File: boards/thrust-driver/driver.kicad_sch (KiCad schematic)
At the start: 33 parts, among them J1 HELM J13 1:1, J2 LUG BATT+, J3 LUG BATT-, J4 LUG MOT A, J5 LUG MOT B, J6 CAN XCVR 3V3, J7 NMEA2000 PWR, U1 BTN8982TA, U2 BTN8982TA, U3 BTN8982TA, U4 BTN8982TA, U5 Pico 2 (DNP), U6 R-78E5.0-0.5 (DNP)

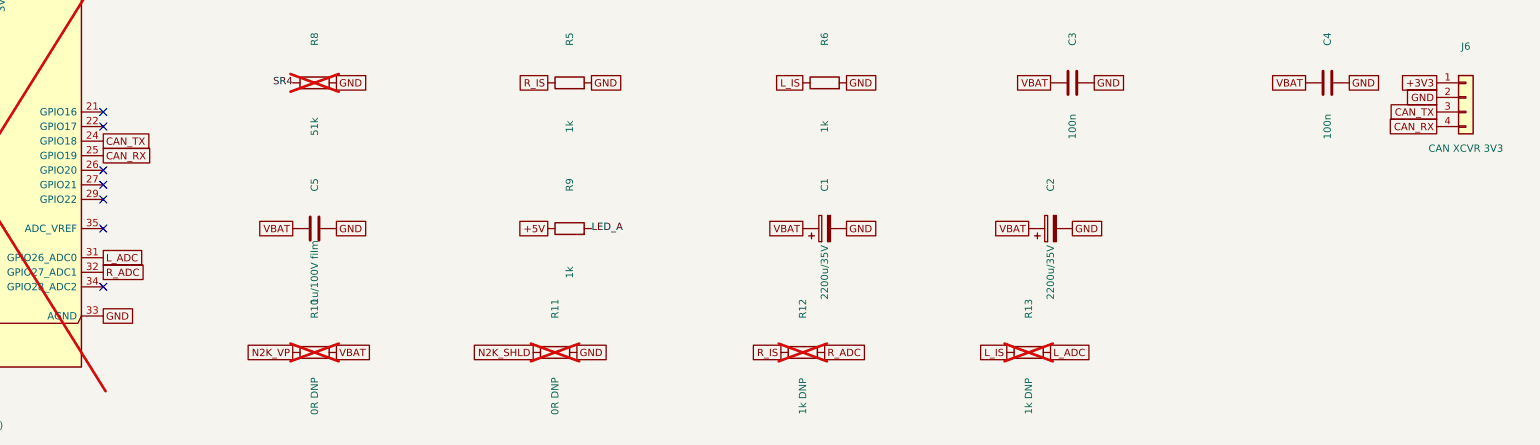
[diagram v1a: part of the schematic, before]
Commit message: feat(schematics): wire the Pico to its peripherals on both boards
Helm control page: GP0-3 bus to J12, 4-wire thrust bus to J13 (nested
staircase under the pico), RPWM/LPWM to the servo bridge inputs,
LED_STAT to R13, VBAT_SENSE over the arrivals down to the divider rail.
Driver page: DNP-pico CAN pair to J6, IS-to-ADC series R12/R13.
gen_sheet.py: turtle-style waypoint routing for WIRES (("x"/"y", v)
segments + auto-L tail); layout shuffle so J12/J13 flank the pico.

Co-Authored-By: Claude Fable 5 <noreply@anthropic.com>
Claude-Session: https://claude.ai/code/session_011PT4Xv5KGhDdDc8nqJyMxJ
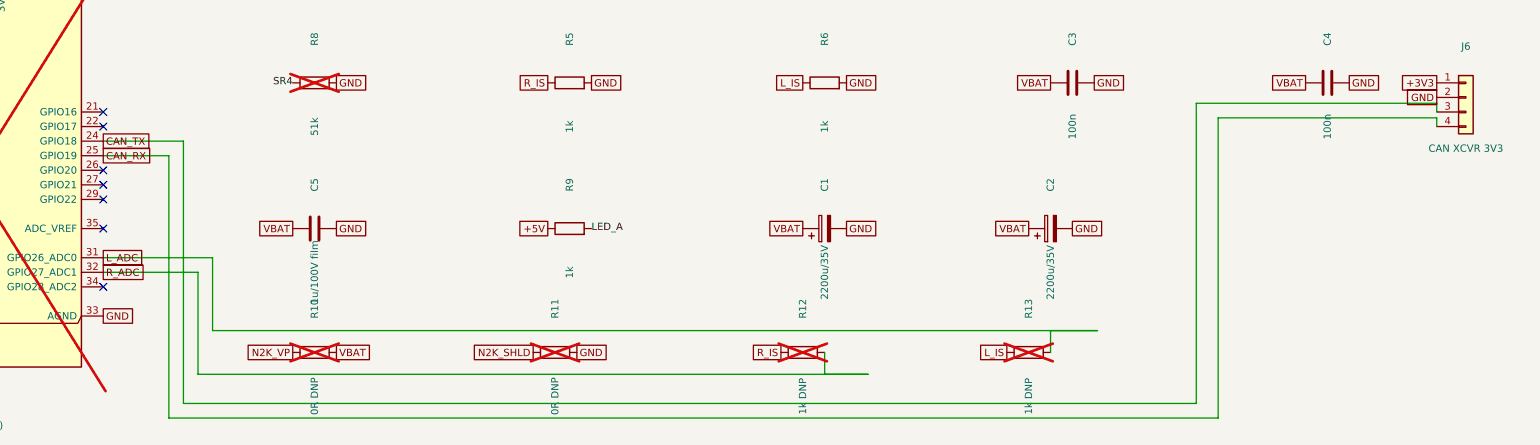
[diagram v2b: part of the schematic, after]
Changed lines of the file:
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@@
     (instances (project "vanchor-thrust" (path "/d0000000-0000-4000-8000-000000000001/d0000000-0000-4000-8000-000000000002" (reference "#FLG03") (unit 1))))
   )
+  (wire (pts (xy 92.71 229.87) (xy 106.68 229.87))
+    (stroke (width 0) (type default)))
+  (wire (pts (xy 106.68 229.87) (xy 106.68 275.59))
+    (stroke (width 0) (type default)))
+  (wire (pts (xy 106.68 275.59) (xy 283.21 275.59))
+    (stroke (width 0) (type default)))
+  (wire (pts (xy 283.21 275.59) (xy 283.21 223.27))
+    (stroke (width 0) (type default)))
+  (wire (pts (xy 283.21 223.27) (xy 325.12 223.27))
+    (stroke (width 0) (type default)))
+  (wire (pts (xy 325.12 223.27) (xy 325.12 224.79))
+    (stroke (width 0) (type default)))
+  (wire (pts (xy 92.71 232.41) (xy 104.14 232.41))
+    (stroke (width 0) (type default)))
+  (wire (pts (xy 104.14 232.41) (xy 104.14 278.13))
+    (stroke (width 0) (type default)))
+  (wire (pts (xy 104.14 278.13) (xy 287.02 278.13))
+    (stroke (width 0) (type default)))
+  (wire (pts (xy 287.02 278.13) (xy 287.02 225.81))
+    (stroke (width 0) (type default)))
+  (wire (pts (xy 287.02 225.81) (xy 325.12 225.81))
+    (stroke (width 0) (type default)))
+  (wire (pts (xy 325.12 225.81) (xy 325.12 227.33))
+    (stroke (width 0) (type default)))
+  (wire (pts (xy 92.71 250.19) (xy 111.76 250.19))
+    (stroke (width 0) (type default)))
+  (wire (pts (xy 111.76 250.19) (xy 111.76 262.89))
+    (stroke (width 0) (type default)))
+  (wire (pts (xy 111.76 262.89) (xy 266 262.89))
+    (stroke (width 0) (type default)))
+  (wire (pts (xy 266 262.89) (xy 257.81 262.89))
+    (stroke (width 0) (type default)))
+  (wire (pts (xy 257.81 262.89) (xy 257.81 266.7))
+    (stroke (width 0) (type default)))
+  (wire (pts (xy 92.71 252.73) (xy 109.22 252.73))
+    (stroke (width 0) (type default)))
+  (wire (pts (xy 109.22 252.73) (xy 109.22 270.51))
+    (stroke (width 0) (type default)))
+  (wire (pts (xy 109.22 270.51) (xy 226 270.51))
+    (stroke (width 0) (type default)))
+  (wire (pts (xy 226 270.51) (xy 218.44 270.51))
+    (stroke (width 0) (type default)))
+  (wire (pts (xy 218.44 270.51) (xy 218.44 266.7))
+    (stroke (width 0) (type default)))
   (global_label "RPWM" (shape passive) (at 39.37 87.63 180.0) (fields_autoplaced yes)
     (effects (font (size 1.27 1.27)) (justify right))
@@
       (effects (font (size 1.27 1.27)) (hide yes)))
   )
-  (global_label "CAN_TX" (shape passive) (at 325.12 224.79 180.0) (fields_autoplaced yes)
-    (effects (font (size 1.27 1.27)) (justify right))
-    (property "Intersheetrefs" "${INTERSHEET_REFS}" (at 325.12 224.79 0)
-      (effects (font (size 1.27 1.27)) (hide yes)))
-  )
-  (global_label "CAN_RX" (shape passive) (at 325.12 227.33 180.0) (fields_autoplaced yes)
-    (effects (font (size 1.27 1.27)) (justify right))
-    (property "Intersheetrefs" "${INTERSHEET_REFS}" (at 325.12 227.33 0)
-      (effects (font (size 1.27 1.27)) (hide yes)))
-  )
   (global_label "N2K_VP" (shape passive) (at 368.3 219.71 180.0) (fields_autoplaced yes)
     (effects (font (size 1.27 1.27)) (justify right))
@@
       (effects (font (size 1.27 1.27)) (hide yes)))
   )
-  (global_label "R_ADC" (shape passive) (at 218.44 266.7 0.0) (fields_autoplaced yes)
-    (effects (font (size 1.27 1.27)) (justify left))
-    (property "Intersheetrefs" "${INTERSHEET_REFS}" (at 218.44 266.7 0)
-      (effects (font (size 1.27 1.27)) (hide yes)))
-  )
   (global_label "L_IS" (shape passive) (at 250.19 266.7 180.0) (fields_autoplaced yes)
     (effects (font (size 1.27 1.27)) (justify right))
@@
       (effects (font (size 1.27 1.27)) (hide yes)))
   )
-  (global_label "L_ADC" (shape passive) (at 257.81 266.7 0.0) (fields_autoplaced yes)
-    (effects (font (size 1.27 1.27)) (justify left))
-    (property "Intersheetrefs" "${INTERSHEET_REFS}" (at 257.81 266.7 0)
-      (effects (font (size 1.27 1.27)) (hide yes)))
-  )

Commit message: fix(schematics): visual QA pass — text collisions and wire-through-symbol
gen_sheet: BAT54S ref+value stack below the part (COM pin label owns the
space above — fixes D8/D10/D11/D14 overprinted refs); REF_POS per-part
ref override. Carrier: F1->Q1 drain wire enters from above instead of
through the FET symbol; Q1 ref moved clear. Control: R20/R21 spread so
their texts don't merge; D14 lifted off the VBAT wire; LED_STAT run
raised above the pico power flags. Driver: ADC wires lose their dead-end
spurs; CAN lanes dropped below the DNP value texts; D2 horizontal (label
was overprinting ref/value). HANDOFF: waive note for the 3 paralleled-OUT
ERC errors. Netlists verified identical on both boards.

Co-Authored-By: Claude Fable 5 <noreply@anthropic.com>
Claude-Session: https://claude.ai/code/session_011PT4Xv5KGhDdDc8nqJyMxJ
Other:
- moved on the sheet: D2
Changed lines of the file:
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@@
     (instances (project "vanchor-thrust" (path "/d0000000-0000-4000-8000-000000000001/d0000000-0000-4000-8000-000000000002" (reference "R6") (unit 1))))
   )
-  (symbol (lib_id "Device:D_TVS") (at 330.2 191.77 90) (unit 1)
-    (exclude_from_sim no) (in_bom yes) (on_board yes) (dnp no)
-    (property "Reference" "D2" (at 330.2 184.15 0)
-      (effects (font (size 1.27 1.27))))
-    (property "Value" "SMCJ33A" (at 330.2 199.39 0)
-      (effects (font (size 1.27 1.27))))
-    (property "Footprint" "Diode_SMD:D_SMC" (at 330.2 191.77 0)
-      (effects (font (size 1.27 1.27)) (hide yes)))
-    (property "Datasheet" "" (at 330.2 191.77 0)
+  (symbol (lib_id "Device:D_TVS") (at 322.58 190.5 0) (unit 1)
+    (exclude_from_sim no) (in_bom yes) (on_board yes) (dnp no)
+    (property "Reference" "D2" (at 322.58 182.88 0)
+      (effects (font (size 1.27 1.27))))
+    (property "Value" "SMCJ33A" (at 322.58 198.12 0)
+      (effects (font (size 1.27 1.27))))
+    (property "Footprint" "Diode_SMD:D_SMC" (at 322.58 190.5 0)
+      (effects (font (size 1.27 1.27)) (hide yes)))
+    (property "Datasheet" "" (at 322.58 190.5 0)
       (effects (font (size 1.27 1.27)) (hide yes)))
     (pin "1")
@@
   (wire (pts (xy 92.71 229.87) (xy 106.68 229.87))
     (stroke (width 0) (type default)))
-  (wire (pts (xy 106.68 229.87) (xy 106.68 275.59))
-    (stroke (width 0) (type default)))
-  (wire (pts (xy 106.68 275.59) (xy 283.21 275.59))
-    (stroke (width 0) (type default)))
-  (wire (pts (xy 283.21 275.59) (xy 283.21 223.27))
+  (wire (pts (xy 106.68 229.87) (xy 106.68 280.67))
+    (stroke (width 0) (type default)))
+  (wire (pts (xy 106.68 280.67) (xy 283.21 280.67))
+    (stroke (width 0) (type default)))
+  (wire (pts (xy 283.21 280.67) (xy 283.21 223.27))
     (stroke (width 0) (type default)))
   (wire (pts (xy 283.21 223.27) (xy 325.12 223.27))
@@
   (wire (pts (xy 92.71 232.41) (xy 104.14 232.41))
     (stroke (width 0) (type default)))
-  (wire (pts (xy 104.14 232.41) (xy 104.14 278.13))
-    (stroke (width 0) (type default)))
-  (wire (pts (xy 104.14 278.13) (xy 287.02 278.13))
-    (stroke (width 0) (type default)))
-  (wire (pts (xy 287.02 278.13) (xy 287.02 225.81))
+  (wire (pts (xy 104.14 232.41) (xy 104.14 283.21))
+    (stroke (width 0) (type default)))
+  (wire (pts (xy 104.14 283.21) (xy 287.02 283.21))
+    (stroke (width 0) (type default)))
+  (wire (pts (xy 287.02 283.21) (xy 287.02 225.81))
     (stroke (width 0) (type default)))
   (wire (pts (xy 287.02 225.81) (xy 325.12 225.81))
@@
   (wire (pts (xy 111.76 250.19) (xy 111.76 262.89))
     (stroke (width 0) (type default)))
-  (wire (pts (xy 111.76 262.89) (xy 266 262.89))
-    (stroke (width 0) (type default)))
-  (wire (pts (xy 266 262.89) (xy 257.81 262.89))
+  (wire (pts (xy 111.76 262.89) (xy 257.81 262.89))
     (stroke (width 0) (type default)))
   (wire (pts (xy 257.81 262.89) (xy 257.81 266.7))
@@
   (wire (pts (xy 92.71 252.73) (xy 109.22 252.73))
     (stroke (width 0) (type default)))
-  (wire (pts (xy 109.22 252.73) (xy 109.22 270.51))
-    (stroke (width 0) (type default)))
-  (wire (pts (xy 109.22 270.51) (xy 226 270.51))
-    (stroke (width 0) (type default)))
-  (wire (pts (xy 226 270.51) (xy 218.44 270.51))
-    (stroke (width 0) (type default)))
-  (wire (pts (xy 218.44 270.51) (xy 218.44 266.7))
+  (wire (pts (xy 109.22 252.73) (xy 109.22 264.16))
+    (stroke (width 0) (type default)))
+  (wire (pts (xy 109.22 264.16) (xy 218.44 264.16))
+    (stroke (width 0) (type default)))
+  (wire (pts (xy 218.44 264.16) (xy 218.44 266.7))
     (stroke (width 0) (type default)))
   (global_label "RPWM" (shape passive) (at 39.37 87.63 180.0) (fields_autoplaced yes)
@@
       (effects (font (size 1.27 1.27)) (hide yes)))
   )
-  (global_label "VBAT" (shape passive) (at 330.2 195.58 270.0) (fields_autoplaced yes)
-    (effects (font (size 1.27 1.27)) (justify left))
-    (property "Intersheetrefs" "${INTERSHEET_REFS}" (at 330.2 195.58 0)
-      (effects (font (size 1.27 1.27)) (hide yes)))
-  )
-  (global_label "GND" (shape passive) (at 330.2 187.96 90.0) (fields_autoplaced yes)
-    (effects (font (size 1.27 1.27)) (justify left))
-    (property "Intersheetrefs" "${INTERSHEET_REFS}" (at 330.2 187.96 0)
-      (effects (font (size 1.27 1.27)) (hide yes)))
-  )
+  (global_label "VBAT" (shape passive) (at 318.77 190.5 180.0) (fields_autoplaced yes)
+    (effects (font (size 1.27 1.27)) (justify right))
+    (property "Intersheetrefs" "${INTERSHEET_REFS}" (at 318.77 190.5 0)
+      (effects (font (size 1.27 1.27)) (hide yes)))
+  )
+  (global_label "GND" (shape passive) (at 326.39 190.5 0.0) (fields_autoplaced yes)
+    (effects (font (size 1.27 1.27)) (justify left))
+    (property "Intersheetrefs" "${INTERSHEET_REFS}" (at 326.39 190.5 0)
+      (effects (font (size 1.27 1.27)) (hide yes)))
+  )
